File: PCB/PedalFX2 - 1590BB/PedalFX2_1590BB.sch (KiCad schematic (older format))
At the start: 12 parts, among them J1 Conn_01x04_Female, T1 ACJS-MHDR, T2 ACJS-MHDR, T3 54-00129

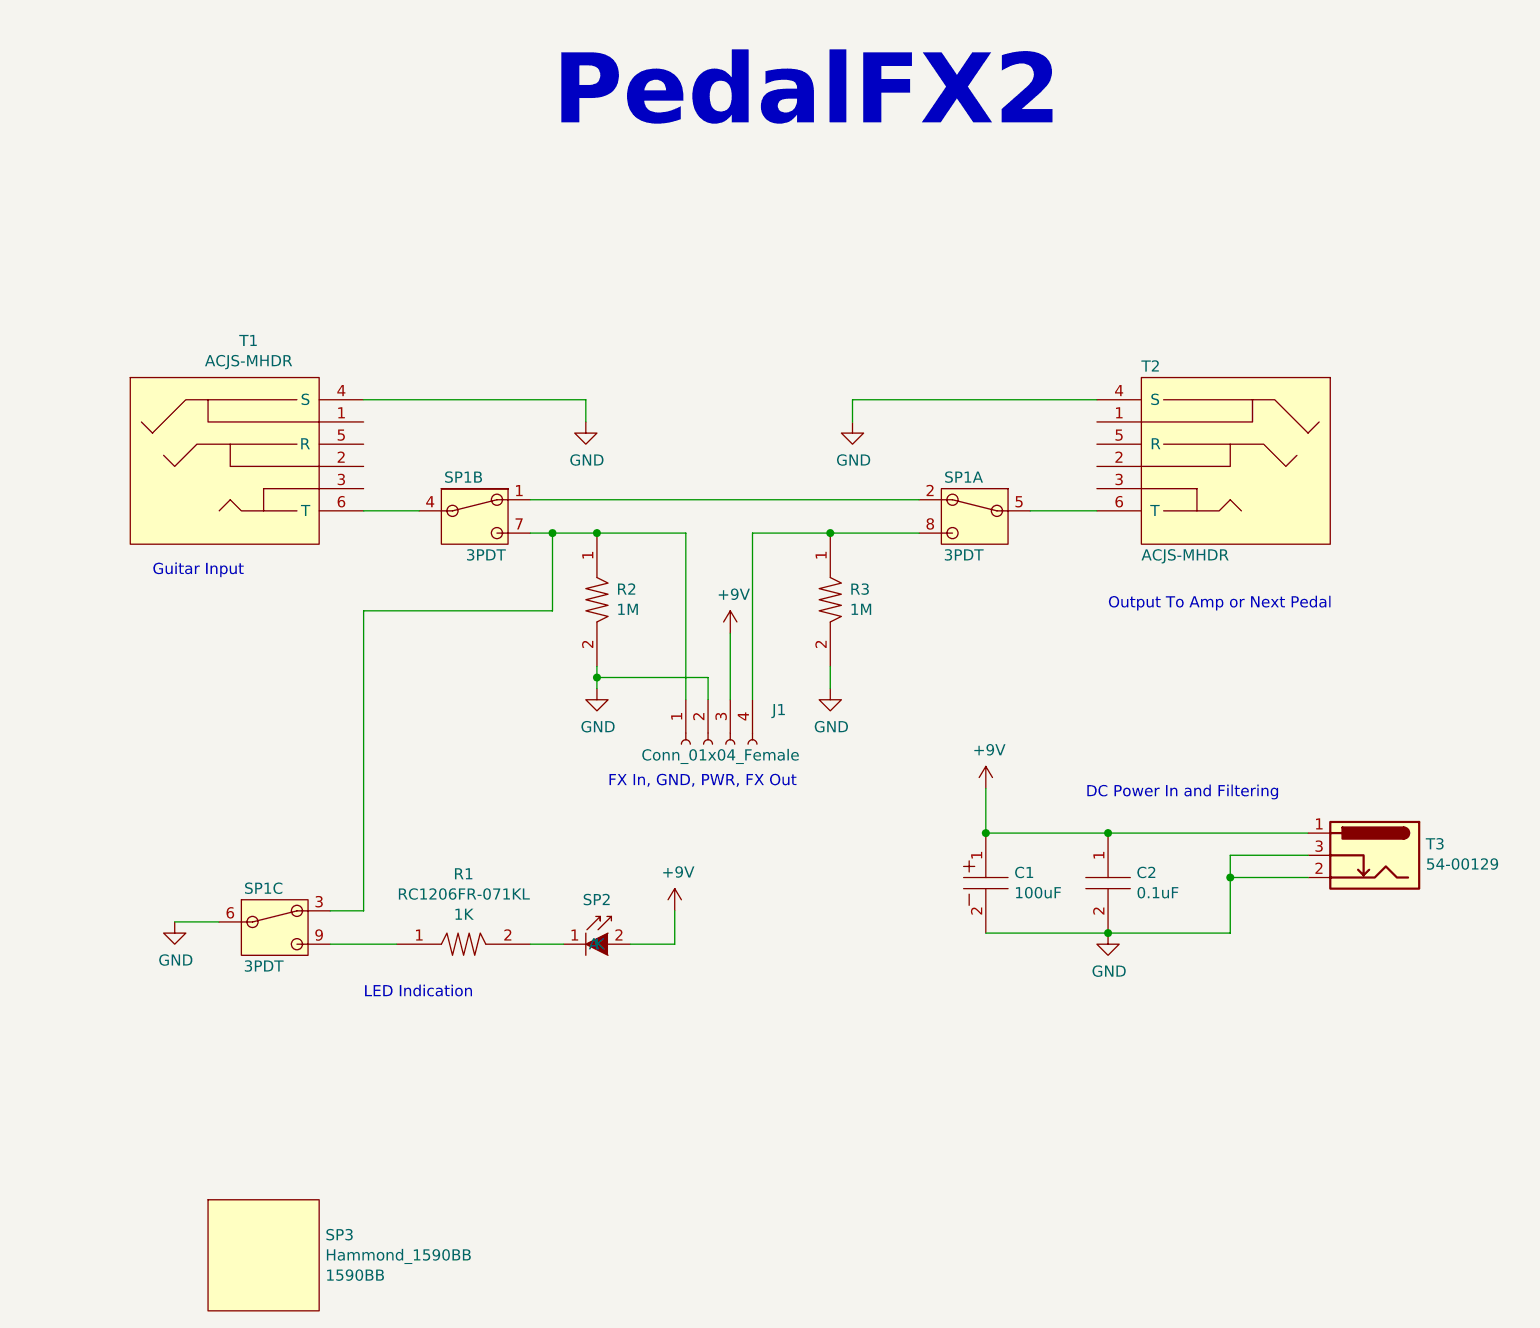
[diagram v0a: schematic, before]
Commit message: Goofed
Goofed internal connector flipped and jacks not flush with housing. All fixed now, all boards redone.
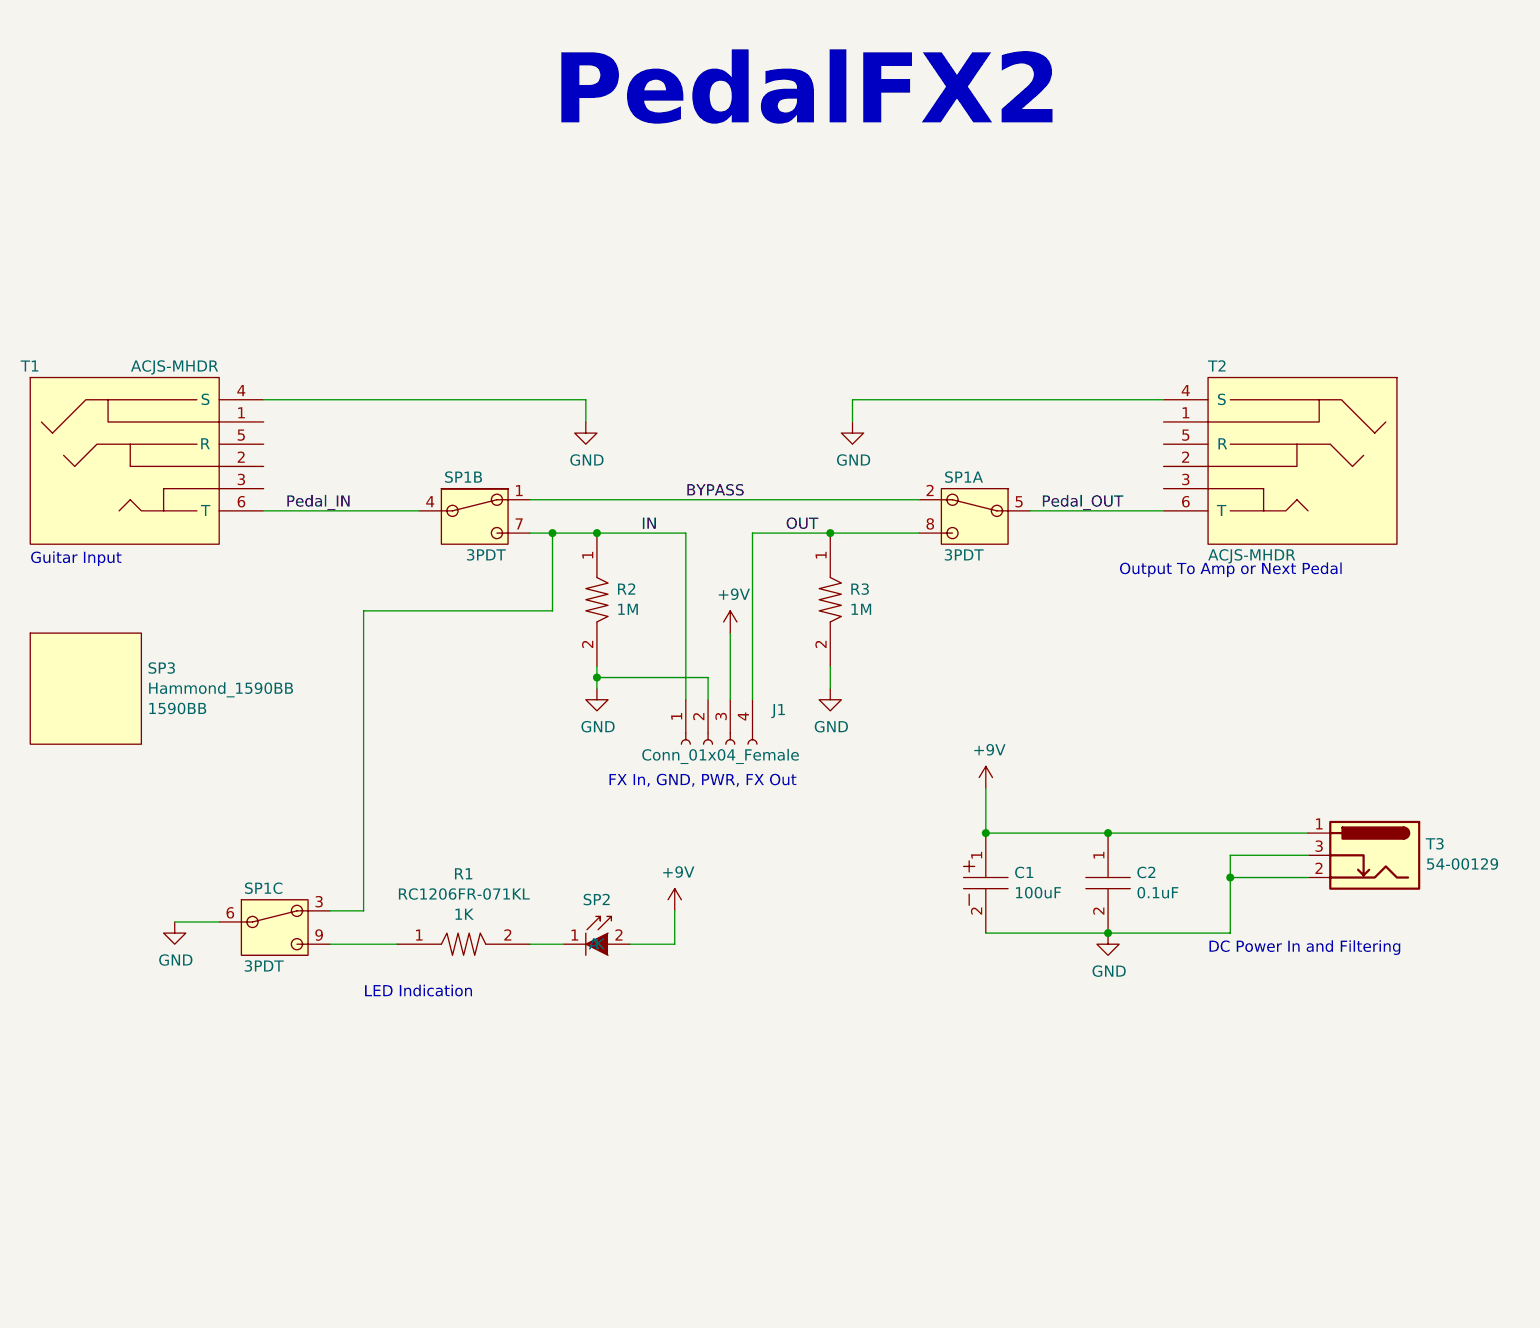
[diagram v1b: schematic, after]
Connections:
- net BYPASS: now reaches SP1.1, SP1.2
- net Pedal_OUT: now reaches SP1.5, T2.6 (T)
- net OUT: now reaches J1.4 (Pin_4), R3.1, SP1.8
- net Pedal_IN: now reaches SP1.4, T1.6 (T)
- net IN: now reaches J1.1 (Pin_1), R2.1, SP1.3, SP1.7
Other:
- moved on the sheet: T1, T2
